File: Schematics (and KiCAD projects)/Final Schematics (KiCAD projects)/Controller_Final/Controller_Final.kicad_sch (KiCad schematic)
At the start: 18 parts, among them J1 OLED_128x64, SW1 RotaryEncoder_Switch, U1 RP2350-ZERO, U2 NRF24L01_Breakout

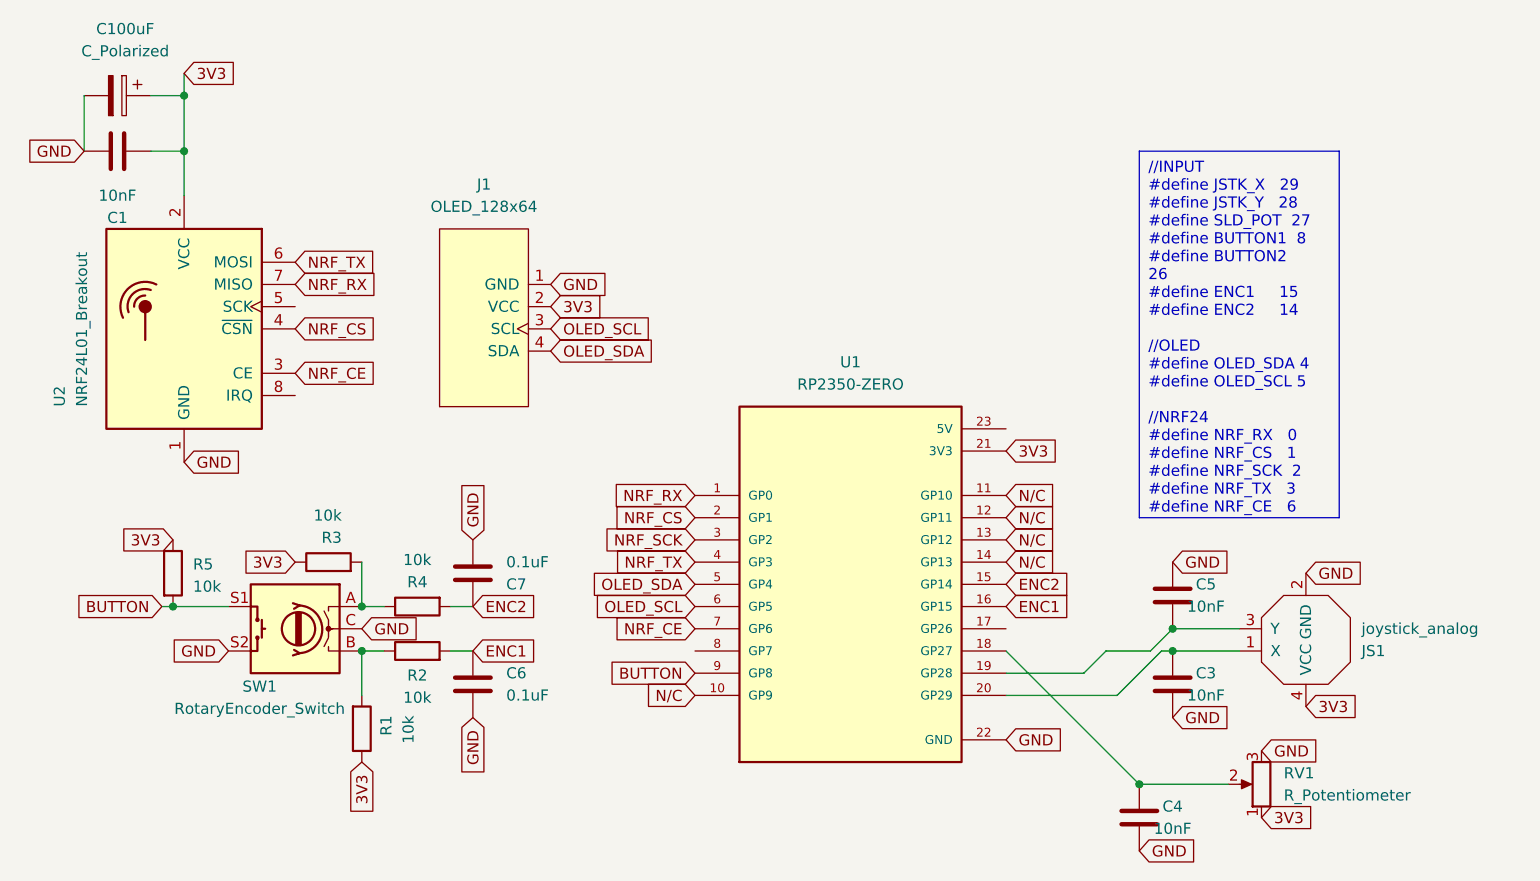
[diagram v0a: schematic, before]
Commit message: updated schematics
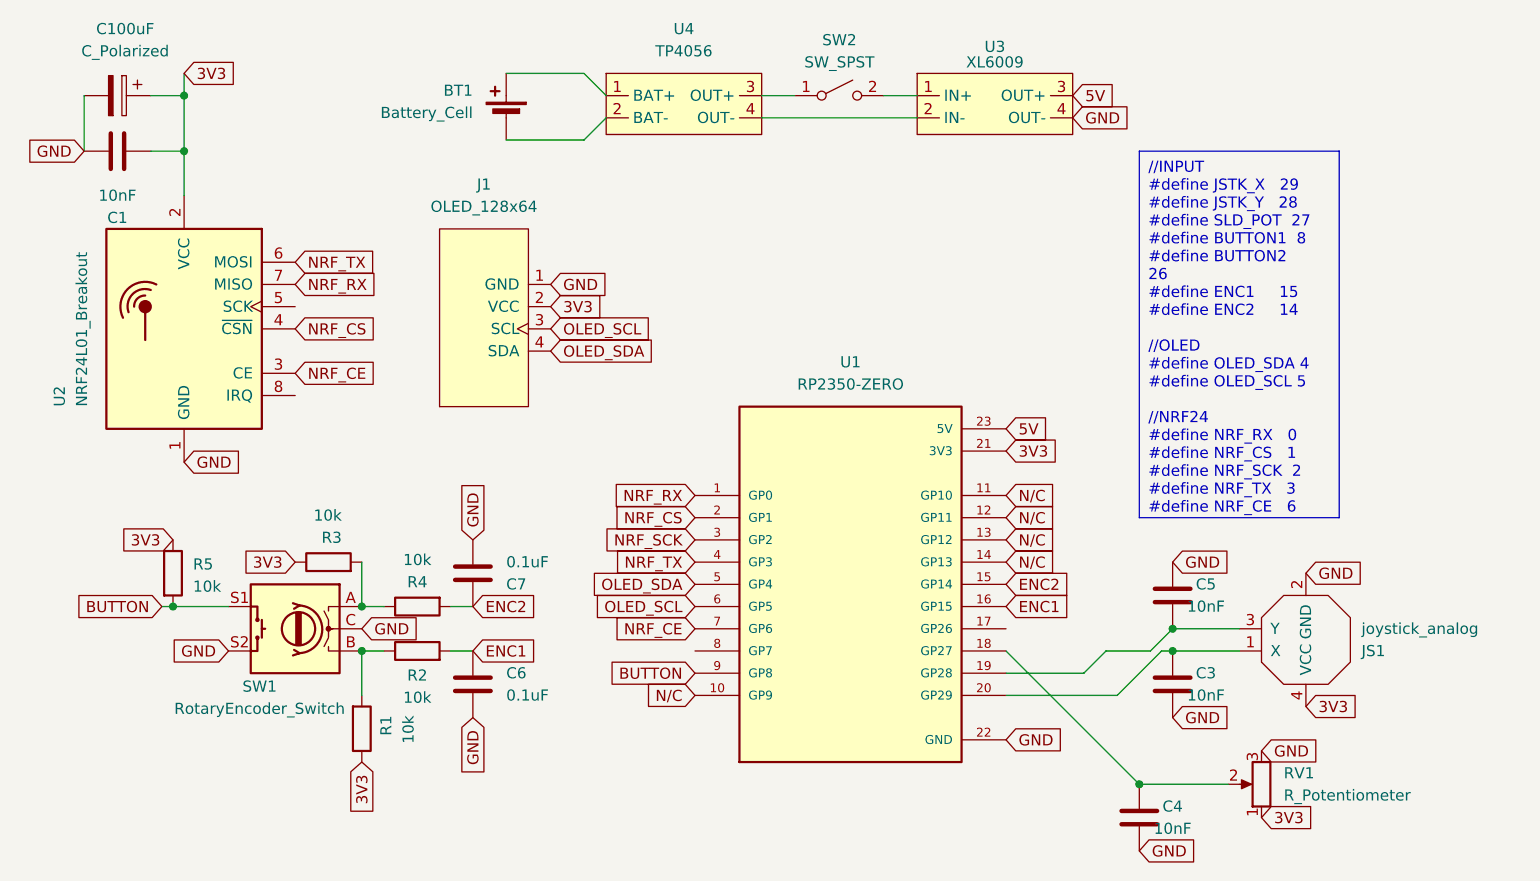
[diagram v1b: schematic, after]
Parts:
- added BT1: Battery_Cell, symbol Device:Battery_Cell
- added SW2: SW_SPST, symbol Switch:SW_SPST
- added U3: XL6009, symbol Misc:XL6009
- added U4: TP4056, symbol Misc:TP4056_Module
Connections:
- net GND: now also U3.4 (OUT-)
- net 5V: now reaches U1.23 (5V)
- net 5V: now also U3.3 (OUT+)
- new net: BT1.1 (+), U4.1 (BAT+)
- new net: BT1.2 (-), U4.2 (BAT-)
- new net: SW2.1 (A), U4.3 (OUT+)
- new net: U3.2 (IN-), U4.4 (OUT-)
- new net: SW2.2 (B), U3.1 (IN+)
